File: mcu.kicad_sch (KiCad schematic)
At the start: 51 parts, among them IC3 RP2040, IC4 AT24C01D-STUM-T, U1 W25Q64JVZPIQ, Y1 7M-12.000MEHE-T

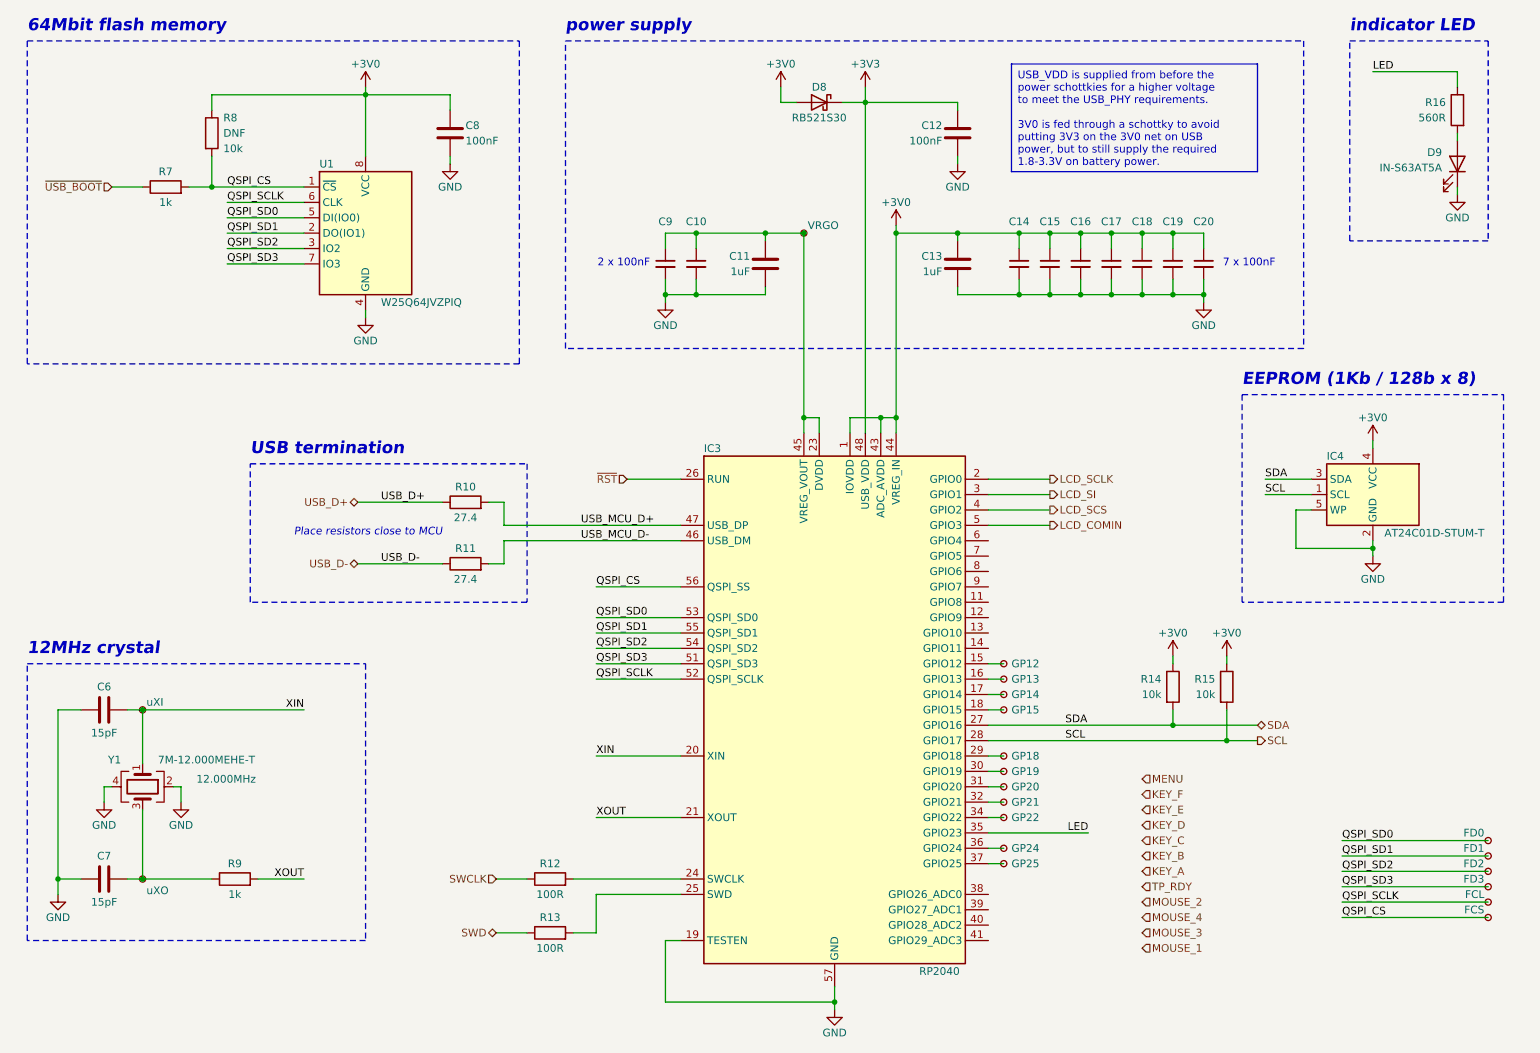
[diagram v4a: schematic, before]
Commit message: pcb done, also kicad 8
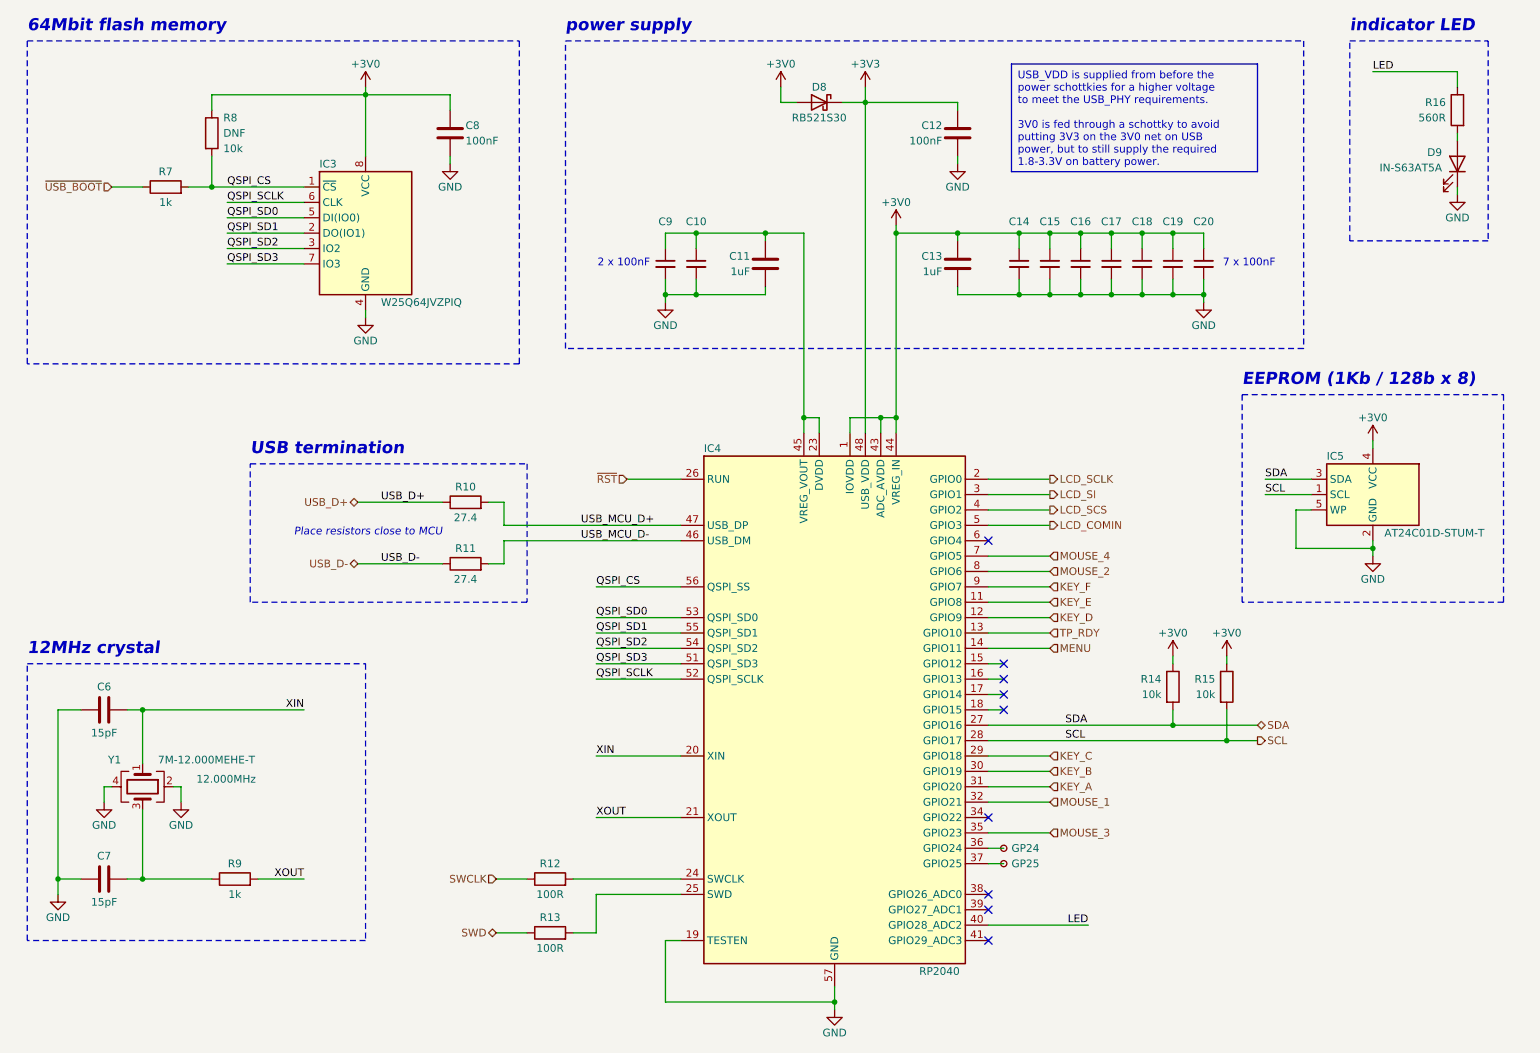
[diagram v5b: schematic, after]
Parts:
- removed TP28: uXI, TestPoint:TestPoint_Pad_D1.0mm, symbol Connector:TestPoint_Small
- removed TP29: uXO, TestPoint:TestPoint_Pad_D1.0mm, symbol Connector:TestPoint_Small
- removed TP30: VRGO, TestPoint:TestPoint_Pad_D1.0mm, symbol Connector:TestPoint_Small
- removed TP31: GP12, TestPoint:TestPoint_Pad_D1.0mm, symbol Connector:TestPoint_Small
- removed TP32: GP13, TestPoint:TestPoint_Pad_D1.0mm, symbol Connector:TestPoint_Small
- removed TP33: GP14, TestPoint:TestPoint_Pad_D1.0mm, symbol Connector:TestPoint_Small
- removed TP34: GP15, TestPoint:TestPoint_Pad_D1.0mm, symbol Connector:TestPoint_Small
- removed TP35: GP18, TestPoint:TestPoint_Pad_D1.0mm, symbol Connector:TestPoint_Small
- removed TP36: GP19, TestPoint:TestPoint_Pad_D1.0mm, symbol Connector:TestPoint_Small
- removed TP37: GP20, TestPoint:TestPoint_Pad_D1.0mm, symbol Connector:TestPoint_Small
- removed TP38: GP21, TestPoint:TestPoint_Pad_D1.0mm, symbol Connector:TestPoint_Small
- removed TP39: GP22, TestPoint:TestPoint_Pad_D1.0mm, symbol Connector:TestPoint_Small
- removed TP40: GP24, TestPoint:TestPoint_Pad_D1.0mm, symbol Connector:TestPoint_Small
- removed TP41: GP25, TestPoint:TestPoint_Pad_D1.0mm, symbol Connector:TestPoint_Small
- removed TP42: FD0, TestPoint:TestPoint_Pad_D1.0mm, symbol Connector:TestPoint_Small
- removed TP43: FD1, TestPoint:TestPoint_Pad_D1.0mm, symbol Connector:TestPoint_Small
- removed TP44: FD2, TestPoint:TestPoint_Pad_D1.0mm, symbol Connector:TestPoint_Small
- removed TP45: FD3, TestPoint:TestPoint_Pad_D1.0mm, symbol Connector:TestPoint_Small
- removed TP46: FCL, TestPoint:TestPoint_Pad_D1.0mm, symbol Connector:TestPoint_Small
- removed TP47: FCS, TestPoint:TestPoint_Pad_D1.0mm, symbol Connector:TestPoint_Small
- added TP4: GP24, TestPoint:TestPoint_Pad_D1.0mm, symbol Connector:TestPoint_Small
- added TP5: GP25, TestPoint:TestPoint_Pad_D1.0mm, symbol Connector:TestPoint_Small
- R14, R15: footprint Resistor_SMD:R_0603_1608Metric -> Resistor_SMD:R_0402_1005Metric
- renumbered U1 to IC3, IC3 to IC4, IC4 to IC5
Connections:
- net KEY_A: now also IC4.31 (GPIO20)
- net KEY_B: now also IC4.30 (GPIO19)
- net KEY_C: now also IC4.29 (GPIO18)
- net KEY_D: now also IC4.12 (GPIO9)
- net KEY_E: now also IC4.11 (GPIO8)
- net KEY_F: now also IC4.9 (GPIO7)
- net LED: now also IC4.40 (GPIO28_ADC2); no longer IC4.35 (GPIO23)
- net MENU: now also IC4.14 (GPIO11)
- net MOUSE_1: now also IC4.32 (GPIO21)
- net MOUSE_2: now also IC4.8 (GPIO6)
- net MOUSE_3: now also IC4.35 (GPIO23)
- net MOUSE_4: now also IC4.7 (GPIO5)
- net TP_RDY: now also IC4.13 (GPIO10)
- net at IC4.36 (GPIO24): now also TP4.1
- net at IC4.37 (GPIO25): now also TP5.1
- no-connect marks 0 -> 9
